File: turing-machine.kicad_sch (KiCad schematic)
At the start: 123 parts, among them J1 Conn_02x05_Odd_Even, J2 cv, J3 clock, J4 out, J5 noise, J6 Conn_02x08_Odd_Even, J7 Conn_02x08_Odd_Even, J8 pulse, Q1 BC547, SW1 SW_Rotary12, SW2 SW_SPDT_MSM, U1 TL072, U10 4050, U11 L78L09_SOT89, U12 4081, U13 4081, U14 TL072, U2 DAC08, U3 TL431DBZ, U4 4016, U5 TL072, U6 4015, U7 4015, U8 L78L09_SOT89, U9 4050

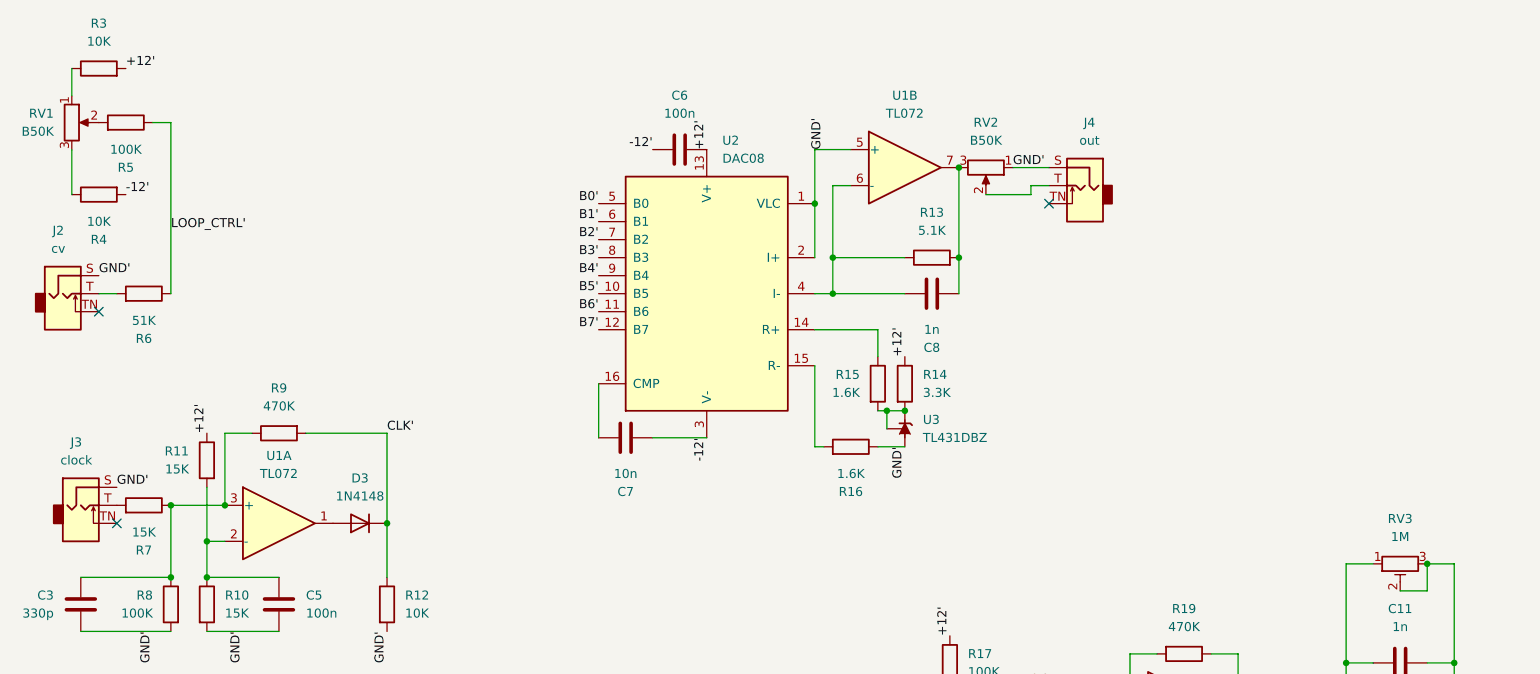
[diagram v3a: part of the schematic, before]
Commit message: ready for v0 manu
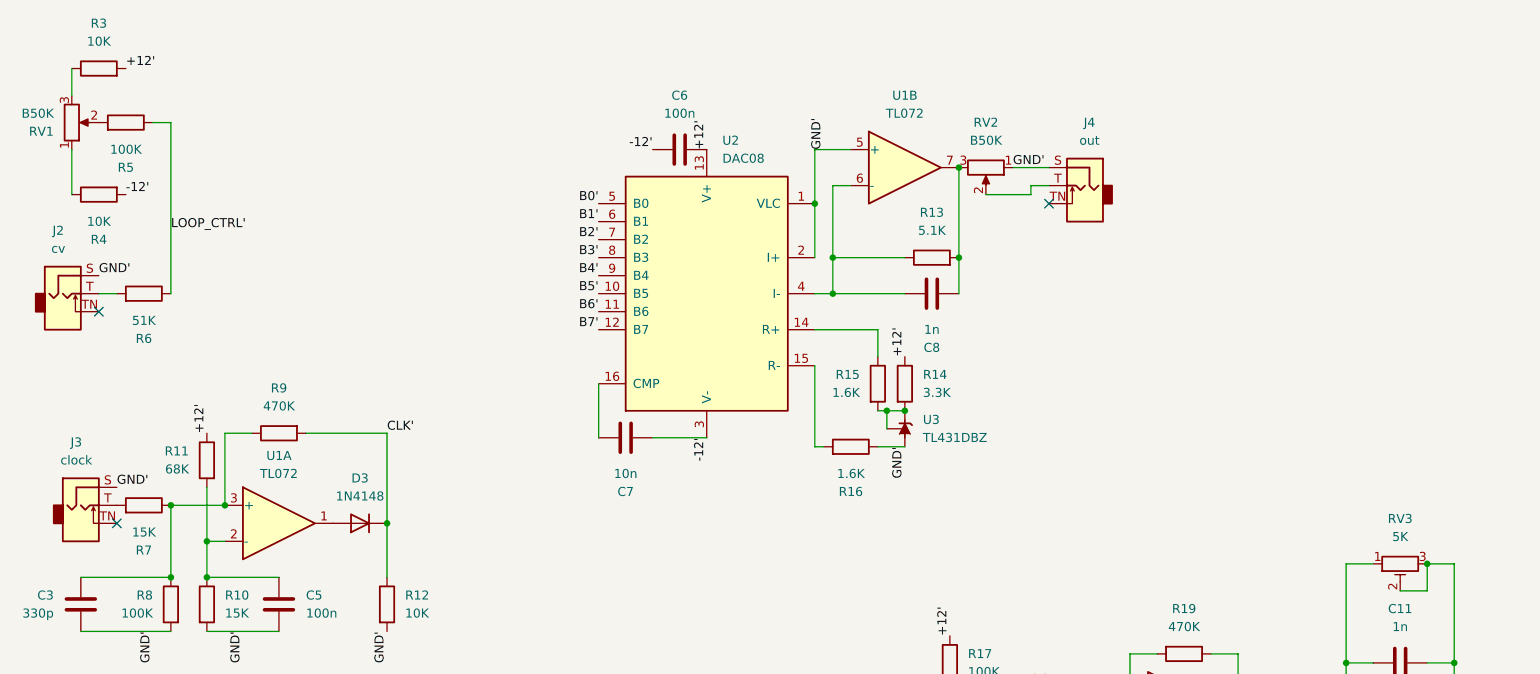
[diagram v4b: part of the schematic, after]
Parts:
- H21: footprint Eurorack:Mech-2M_Switch-Hole -> Eurorack:Mech-1M_Switch-Hole
- R11: value 15K -> 68K
- RV3: value 1M -> 5K
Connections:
- net at RV1.1: now also R4.1; no longer R3.1
- net at RV1.3: now also R3.1; no longer R4.1
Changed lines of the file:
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@@
       (effects (font (size 1.27 1.27)) (justify left))
     )
-    (property "Value" "15K" (at 38.1 78.105 0)
+    (property "Value" "68K" (at 38.1 78.105 0)
       (effects (font (size 1.27 1.27)) (justify left))
     )
@@
       (effects (font (size 1.27 1.27)))
     )
-    (property "Value" "1M" (at 208.915 87.63 90)
+    (property "Value" "5K" (at 208.915 87.63 90)
       (effects (font (size 1.27 1.27)))
     )
@@
     )
   )
-  (symbol (lib_id "Device:R_Potentiometer") (at 21.59 29.21 0) (unit 1)
-    (in_bom yes) (on_board yes) (dnp no) (fields_autoplaced)
-    (property "Reference" "RV1" (at 19.05 27.94 0)
+  (symbol (lib_id "Device:R_Potentiometer") (at 21.59 29.21 0) (mirror x) (unit 1)
+    (in_bom yes) (on_board yes) (dnp no)
+    (property "Reference" "RV1" (at 19.05 30.48 0)
       (effects (font (size 1.27 1.27)) (justify right))
     )
-    (property "Value" "B50K" (at 19.05 30.48 0)
+    (property "Value" "B50K" (at 19.05 27.94 0)
       (effects (font (size 1.27 1.27)) (justify right))
     )
@@
       (effects (font (size 1.27 1.27)) (justify left))
     )
-    (property "Footprint" "Eurorack:Mech-2M_Switch-Hole" (at 50.8 277.495 0)
-      (effects (font (size 1.27 1.27)) hide)
-    )
+    (property "Footprint" "Eurorack:Mech-1M_Switch-Hole" (at 50.8 277.495 0)
+      (effects (font (size 1.27 1.27)) hide)
+    )

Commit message: ready for v1 manu
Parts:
- removed C16, C17, C18: 1n, Capacitor_SMD:C_0805_2012Metric, symbol Device:C
- removed C3: 330p, Capacitor_SMD:C_0805_2012Metric, symbol Device:C
- removed C5: 100n, Capacitor_SMD:C_0805_2012Metric, symbol Device:C
- removed U2: DAC08, Package_SO:SOIC-16_3.9x9.9mm_P1.27mm, symbol Analog_DAC:DAC08
- added D14: 1N4148, Diode_SMD:D_SOD-323_HandSoldering, symbol Device:D
- added H24: trim, Eurorack:Mech-LED-Hole-3mm, symbol Mechanical:MountingHole_Pad
- added Q2: BCM847, Package_SO:TSOP-6_1.65x3.05mm_P0.95mm, symbol Device:Q_Dual_NPN_NPN_E1B1C2E2B2C1
- added R34: 10K, Resistor_SMD:R_0805_2012Metric, symbol Device:R
- added U2: DAC0800_SOIC, Package_SO:SOIC-16_3.9x9.9mm_P1.27mm, symbol Eurorack:DAC0800_SOIC
- R10: value 15K -> 10K
- R11: value 68K -> 100K
- R12: value 10K -> 3.9K
- R30: value 10K -> 68K
- R31: value 10K -> 15K
- R32: value 10K -> 470K
- R7: value 15K -> 100K
- R8: value 100K -> 8.2K
- R9: value 470K -> 470
- renumbered C12 to C10, C13 to C11, C14 to C12, C15 to C13, C4 to C3, C6 to C4, C7 to C5, C8 to C6, C9 to C7, C10 to C8, C11 to C9
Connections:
- net +12V: now also R12.1, R30.2, R8.1, U2.1 (VCC); no longer R11.1
- net -12V: now also C5.1, U2.7 (VEE); no longer C5.2
- net B0': now also U7.7 (D), U2.9 (A1); no longer R31.1
- net B1': now also U2.10 (A2)
- net B2': now also U2.11 (A3)
- net B3': now also U2.12 (A4)
- net B4': now also U6.15 (D), U2.13 (A5); no longer R30.1
- net B5': now also U2.14 (A6)
- net B6': now also U2.15 (A7)
- net B7': now also U2.16 (A8)
- net CLK': now also R32.1, D14.1 (K), R34.2; no longer D3.1 (K), R12.1, R9.2
- net FACE: now also H24.1
- net GND: now also D3.2 (A), R11.2, R31.1, R9.1, R34.1, U2.5 (VLC), U2.6 (GND); no longer R10.2, R12.2, R8.2
- net s12': now also U7.15 (D); no longer R32.1
- net at R14.2, U3.1 (K), U3.2 (REF): now also R15.1; no longer R15.2
- net at C6.1, R13.1, U1.6 (-): now also U2.8 (I0)
- net at R31.2: now also R30.1, U1.2 (-); no longer U7.7 (D)
- net at R32.2: now also R12.2, U1.3 (+), Q2.3 (C2); no longer U7.15 (D)
- net at U1.1: now also D14.2 (A); no longer D3.2 (A)
- net at R16.2: now also U2.3 (VREF-)
- new net: Q2.1 (E1), Q2.4 (E2), R9.2
- new net: Q2.5 (B2), R10.2, R11.1
- new net: R15.2, U2.2 (VREF+)
- new net: C5.2, U2.4 (COMPEN)
- new net: D3.1 (K), Q2.2 (B1), R7.1
- new net: Q2.6 (C1), R10.1, R8.2
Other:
- note added: "Max Clock 1300Hz"
- note added: "Schmitt Trigger with hysteresis"
- note added: "V_HT = 2.4V V_LT = 1.3V"
- moved on the sheet: C4, C5, C6, D3, J4, R10, R11, R12, R13, R14, R15, R16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

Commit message: adding results from troubleshooting
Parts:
- added TP1: RAND, TestPoint:TestPoint_Plated_Hole_D2.0mm, symbol Connector:TestPoint
- added TP2: LOOP_CTRL, TestPoint:TestPoint_Plated_Hole_D2.0mm, symbol Connector:TestPoint
- C12: value 100n -> 1n
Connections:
- net LOOP_CTRL': now also TP2.1
- net RAND': now also TP1.1
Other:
- moved on the sheet: C12, R25, R26, R27, U4A, U4B, U4C, U4D

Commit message: v1a board ready, refit of v1 board available
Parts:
- removed R1, R2: 10, Resistor_SMD:R_0805_2012Metric, symbol Device:R
- added FB1, FB2: 70 Ohm, Inductor_SMD:L_0805_2012Metric, symbol Device:FerriteBead
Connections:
- net at D1.3 (COM): now also FB2.1
- net at J1.1 (Pin_1), J1.2 (Pin_2): now also FB2.2
- net at D2.3 (COM): now also FB1.1
- net at J1.10 (Pin_10), J1.9 (Pin_9): now also FB1.2
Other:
- moved on the sheet: C1, C2
